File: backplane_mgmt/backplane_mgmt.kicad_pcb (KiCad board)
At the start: 2 copper layers, 160 x 100 mm, 84 parts, among them J101 AudioJack3, J201 Backplane, J304 VIn, Q301 SUD19P06-60, Q302 SUD19P06-60, U101 LM833, U203 AT24CS32-SSHM, U301 LDL1117S50R, U302 PTH08T220, U303 INA260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

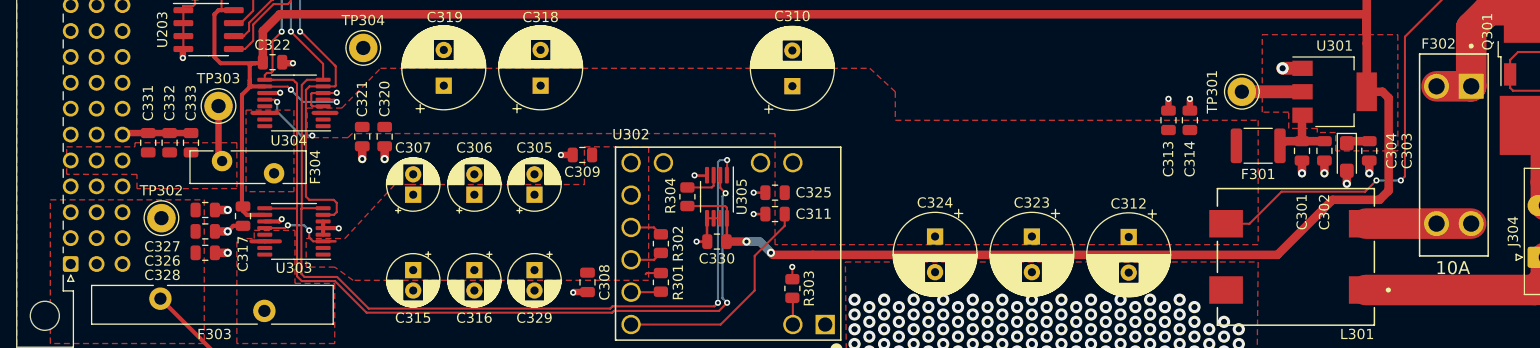
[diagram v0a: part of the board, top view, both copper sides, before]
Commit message: Backplane mechanical improvements
- Added screw holes to the backplane; they may or may not actually be
  correct but the spacing between them should be right. We've got holes
  every two HU's (2x .2") for extra spacing/material between holes

- Added reset LED and some more pull ups

- Minor tweaks to backplane management card
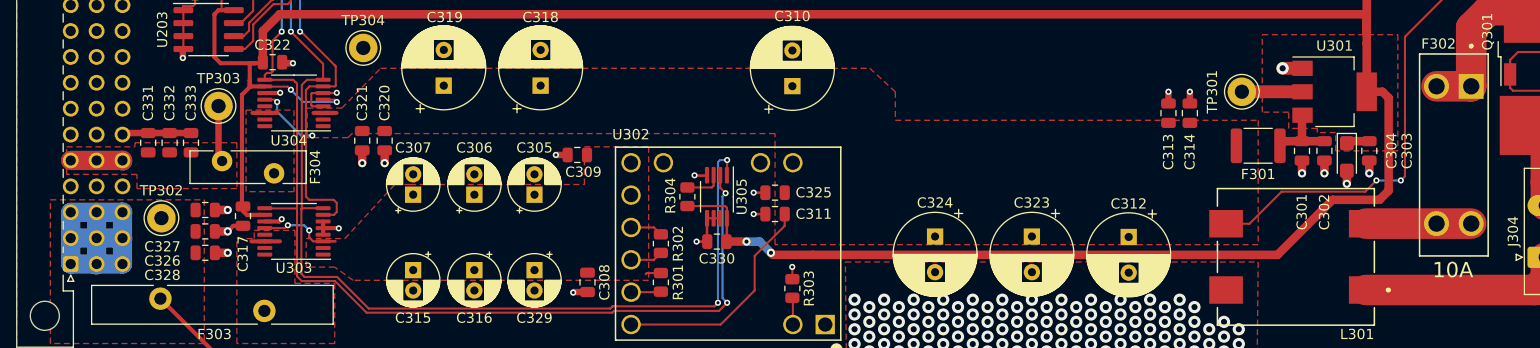
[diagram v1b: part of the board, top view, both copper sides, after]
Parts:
- moved C313 0.70 mm to (143.0, 94.4)
- moved C314 0.70 mm to (145.1, 94.4)
- moved C309 0.50 mm to (85.0, 98.5)
- moved C320 0.40 mm to (66.1, 97.1)
- moved C321 0.40 mm to (63.9, 97.1)
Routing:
- net +5V: track 180.9 -> 211.4 mm
- net +12V: track 5.54 -> 15.8 mm

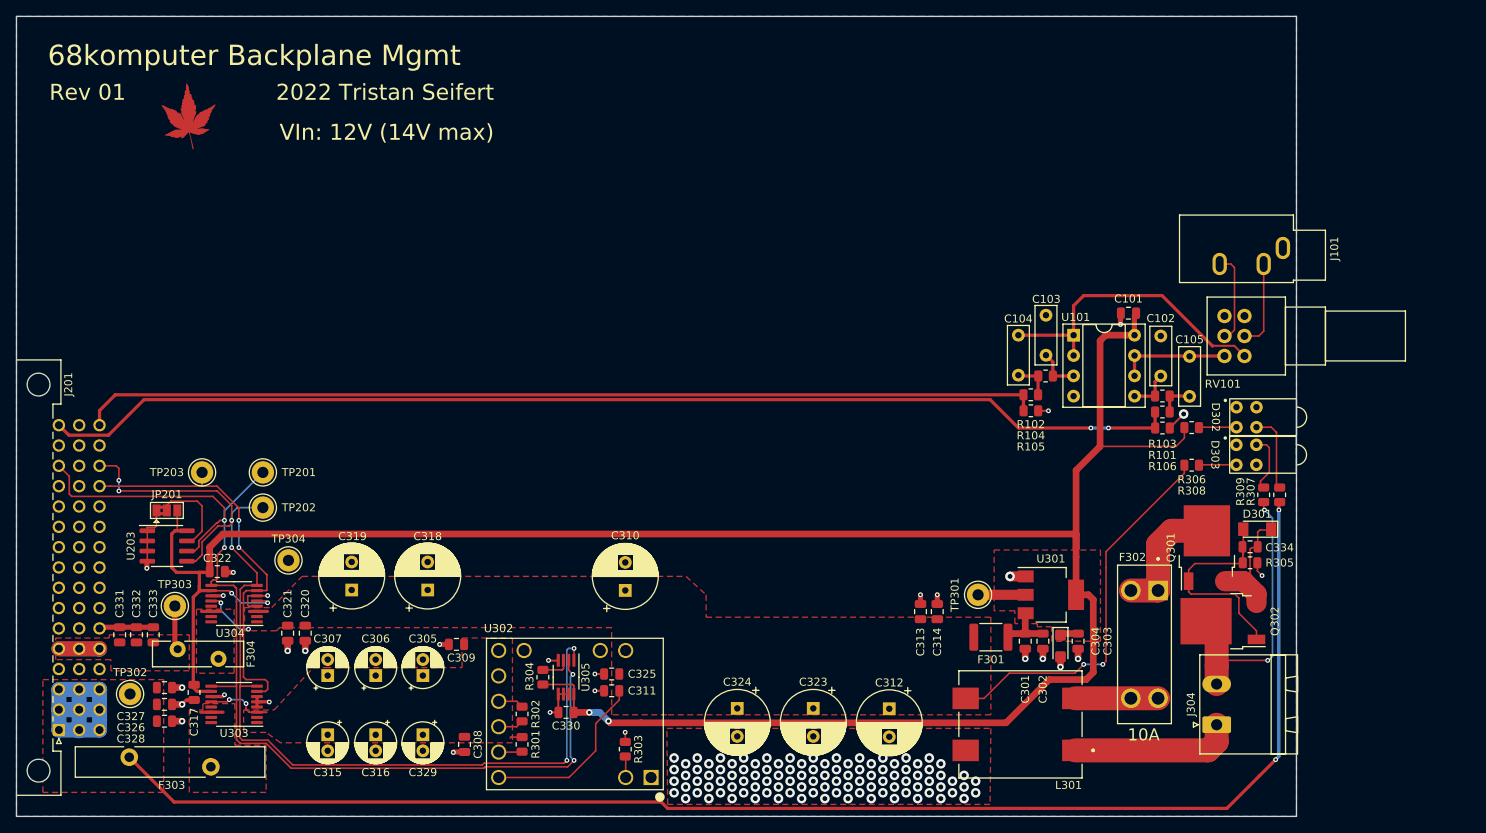
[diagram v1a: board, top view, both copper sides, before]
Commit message: Minor tweaks to all boards
- Moved around some traces on the 68000 CPU card for prettiness

- Added a connector on the backplane to provide +5V/+12V without a
  management card installed (for testing)
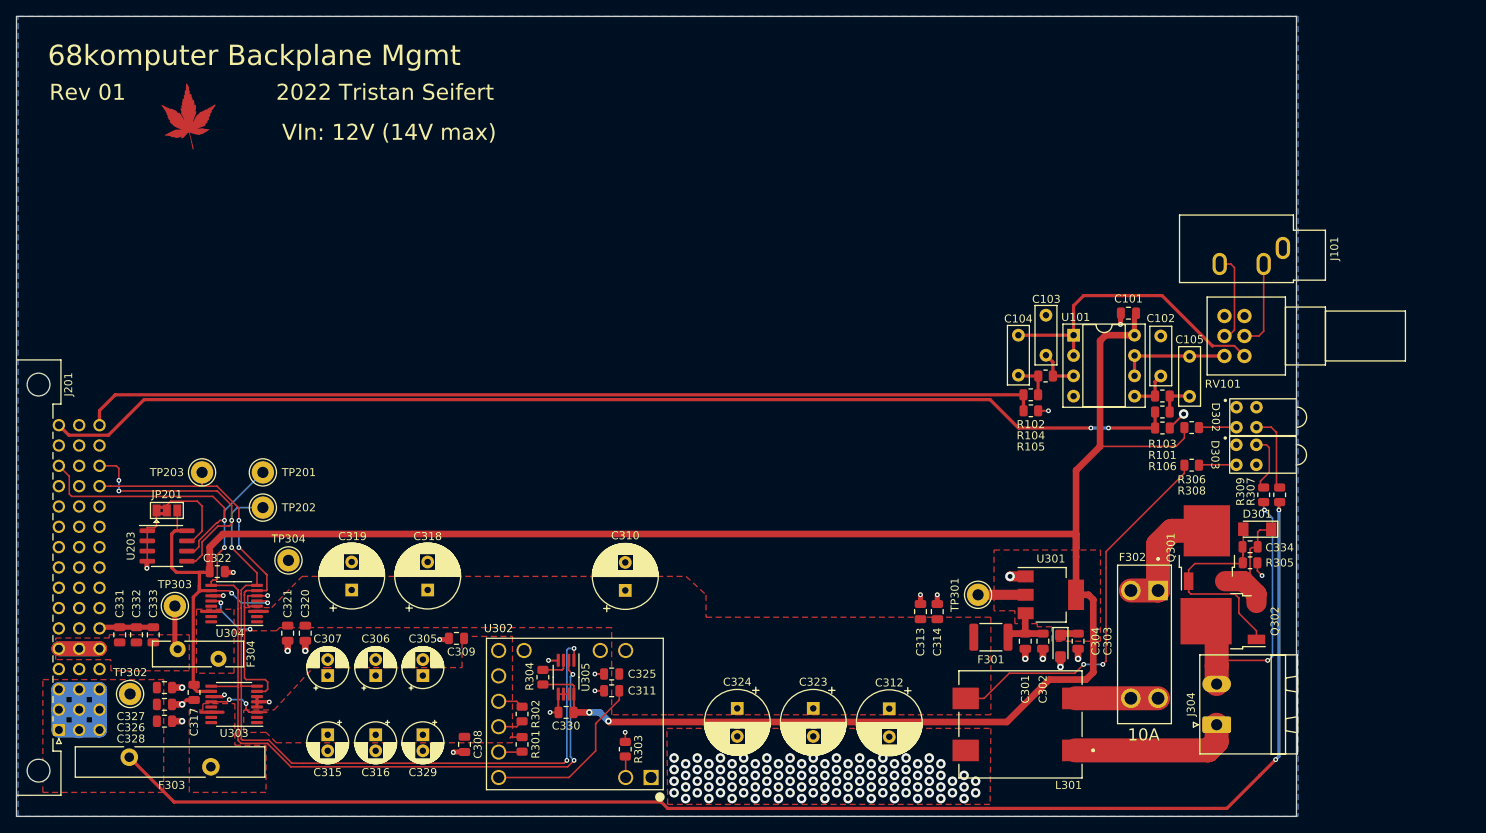
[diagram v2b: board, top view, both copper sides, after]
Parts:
- moved C309 0.75 mm to (85.0, 97.8)
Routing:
- net /SDA: track 127.3 -> 126.7 mm

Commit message: Tweaks to backplane management board
- Added pull downs to the audio inputs, so that if the backplane doesn't
  provide audio, the op amp inputs aren't floating

- Minor tweaks to some of the routing. Also switched out the 5V
  regulator for a larger, easier to get version, and added some large
  planes for power dissapation.
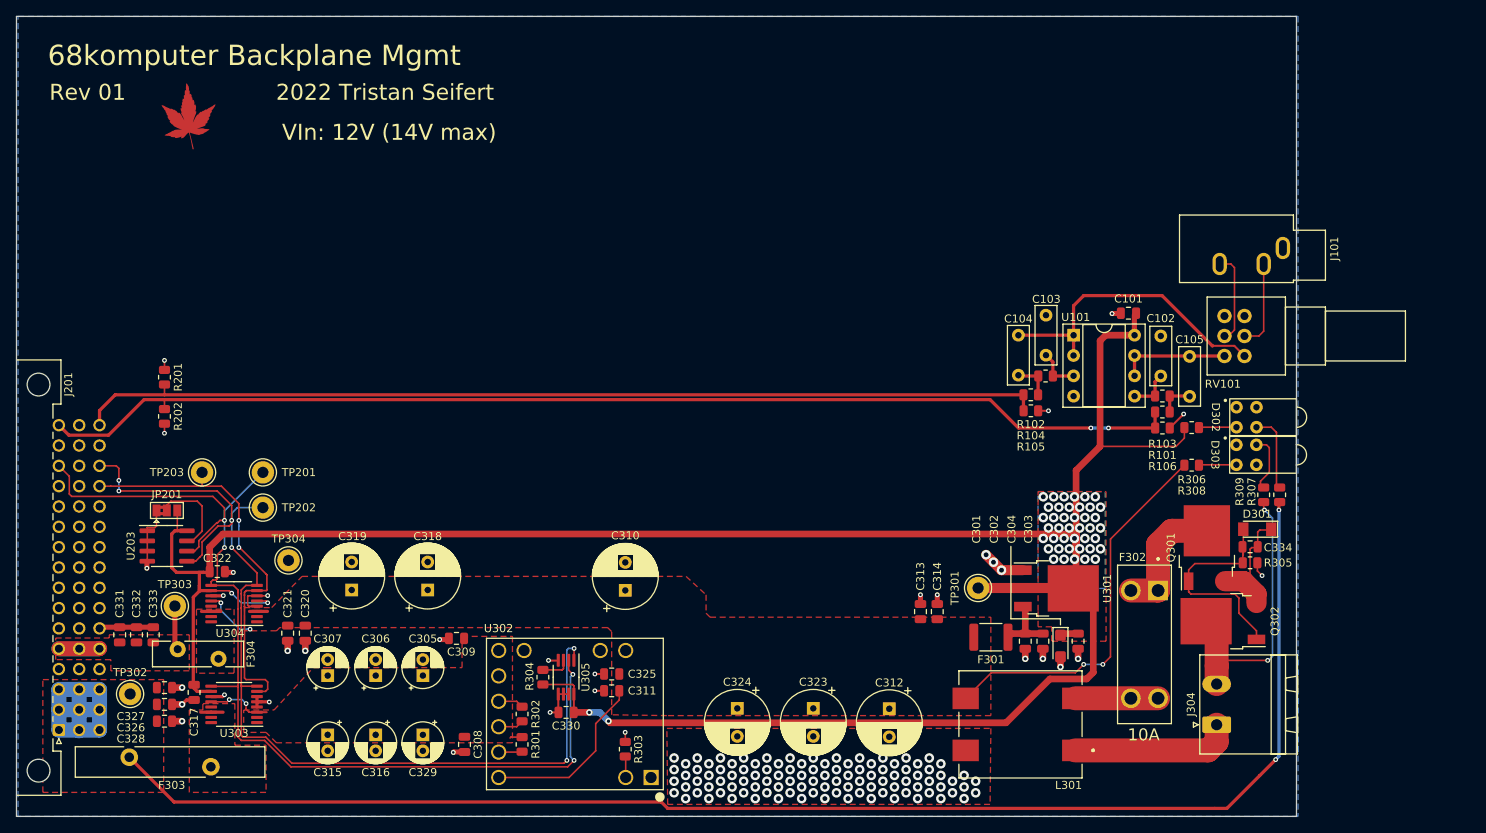
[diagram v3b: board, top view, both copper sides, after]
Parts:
- added R201: 100k, Resistor_SMD:R_0805_2012Metric, F.Cu at (48.5, 65.1)
- added R202: 100k, Resistor_SMD:R_0805_2012Metric, F.Cu at (48.5, 70.0)
- F301: value 140mA -> 100mA
- R305: value 100k -> 1M
- U301: value LDL1117S50R -> AZ1117CD-5.0; footprint Package_TO_SOT_SMD:SOT-223-3_TabPin2 -> Package_TO_SOT_SMD:TO-252-2
- moved U301 1.06 mm to (160.0, 91.5)
- moved TP301 0.85 mm to (150.2, 91.5)
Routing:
- net +5VA: track 304.4 -> 312.5 mm, vias 4 -> 45
- net GND: track 64.1 -> 69.7 mm, vias 132 -> 136
- net /SNDL: track 120.1 -> 121.4 mm
- net /SNDR: track 142.9 -> 144.1 mm
- net Net-(C301-Pad2): track 7.12 -> 8.09 mm
- added copper zone on B.Cu, net +5VA

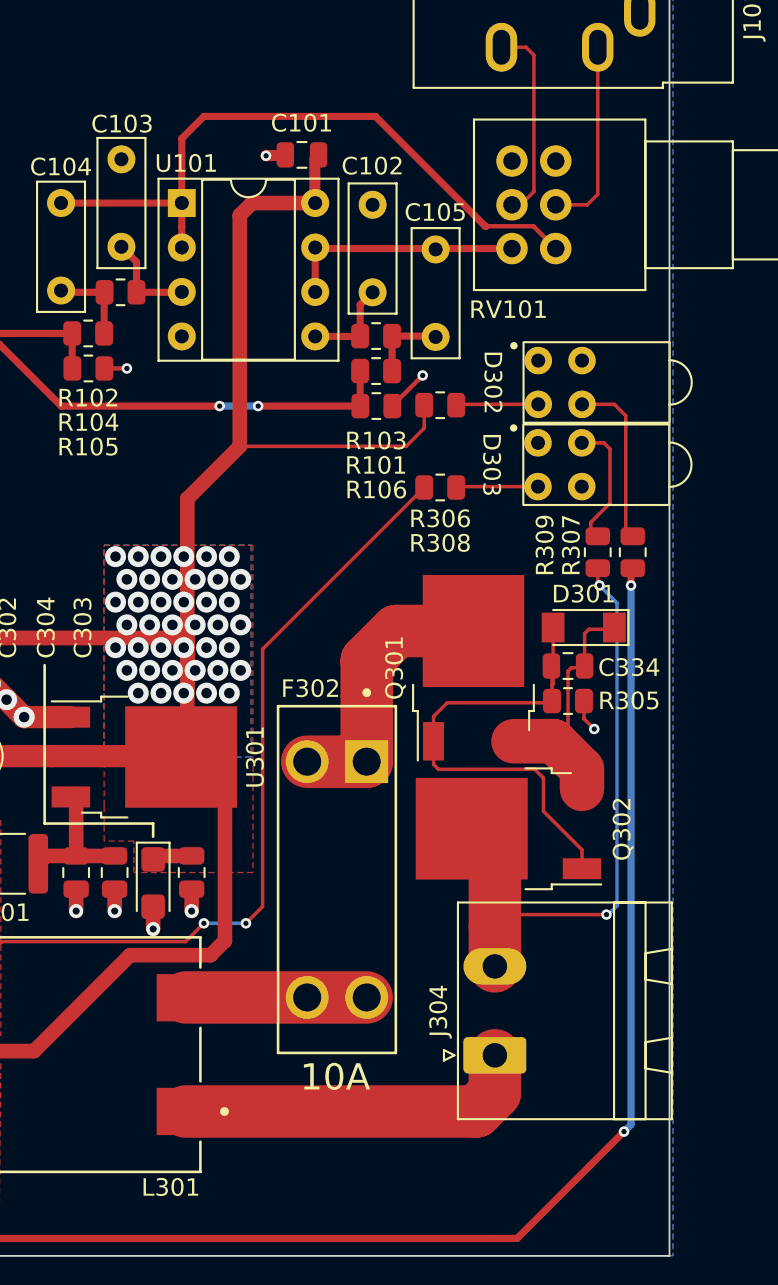
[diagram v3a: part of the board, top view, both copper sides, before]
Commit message: Minor tweaks to power board
- Reorganized the layout of input protection to accomodate a different
  (cheaper) input connector; also added some better thermal dissipation
  for the protection MOSFETs.
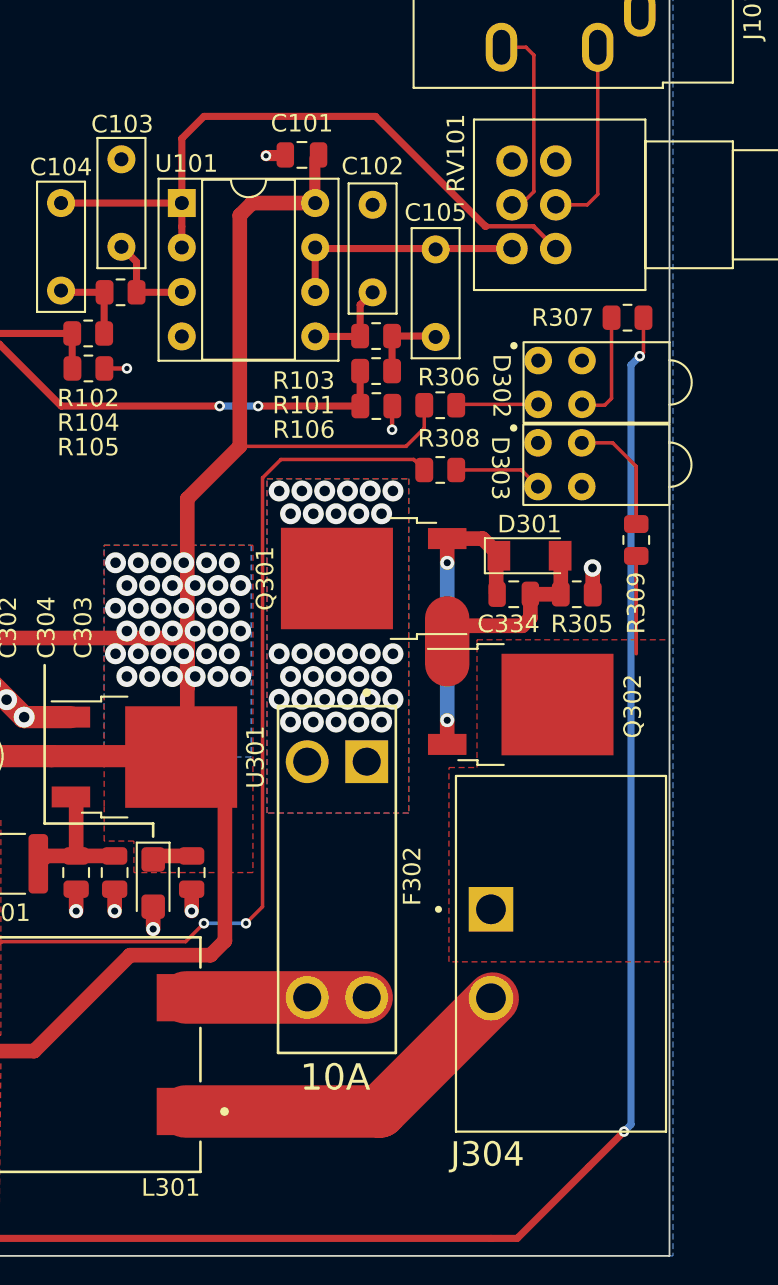
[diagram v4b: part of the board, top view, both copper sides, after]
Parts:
- J304: footprint Connector_Phoenix_MSTB:PhoenixContact_MSTBA_2,5_2-G-5,08_1x02_P5.08mm_Horizontal -> 68komputer-common:CUI_TBP01R1W-508-02BE
- moved R307 13.4 mm to (187.6, 66.4), turned to 0 degrees
- moved J304 8.34 mm to (179.8, 100.2), turned to -90 degrees
- moved Q301 7.65 mm to (173.1, 81.3), turned to 180 degrees
- moved Q302 7.13 mm to (181.5, 88.5), turned to 0 degrees
- moved R305 6.12 mm to (184.7, 82.2)
- moved C334 5.14 mm to (181.1, 82.2), turned to 0 degrees
- moved D301 5.14 mm to (182.0, 80.0), turned to 0 degrees
- moved R309 2.31 mm to (188.1, 79.1)
- moved R308 1.00 mm to (176.9, 75.1)
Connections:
- J304 pad 1: Net-(J304-Pad1) -> /Power/VIn
- J304 pad 2: /Power/VIn -> Net-(L301-Pad1)
- L301 pad 1: Net-(J304-Pad1) -> Net-(L301-Pad1)
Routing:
- net /Power/VIn: track 35.6 -> 5.59 mm, vias 2 -> 0
- net Net-(J304-Pad1): track 20.3 -> 0.00 mm
- net Net-(L301-Pad1): track 0.00 -> 20.2 mm
- net Net-(F302-Pad1): track 16.0 -> 0.00 mm, vias 0 -> 33
- net Net-(C334-Pad2): track 27.8 -> 12.9 mm
- net +5V: track 211.3 -> 225.9 mm
- net VBUS: track 79.4 -> 86.0 mm
- net Net-(D302-Pad1): track 9.56 -> 6.46 mm
- net Net-(C334-Pad1): track 14.8 -> 17.3 mm, vias 0 -> 2
- net GND: track 69.7 -> 68.3 mm
- net +5VA: track 312.5 -> 312.3 mm, vias 45 -> 40
- added copper zone on F.Cu, net /Power/VIn
- added copper zone on B.Cu, net Net-(F302-Pad1)
- added copper zone on F.Cu, net Net-(F302-Pad1)
